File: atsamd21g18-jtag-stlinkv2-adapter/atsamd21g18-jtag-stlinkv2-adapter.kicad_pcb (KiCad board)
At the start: 2 copper layers, 31.8 x 35.6 mm, 4 parts, among them J1 JTAG, J2 HEADER-MALE-10POS-TH-2x5-P0.1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, J3 HEADER-MALE-5POS-TH-1x05-P0.1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, J4 HEADER-MALE-10POS-TH-2x5-P1.2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

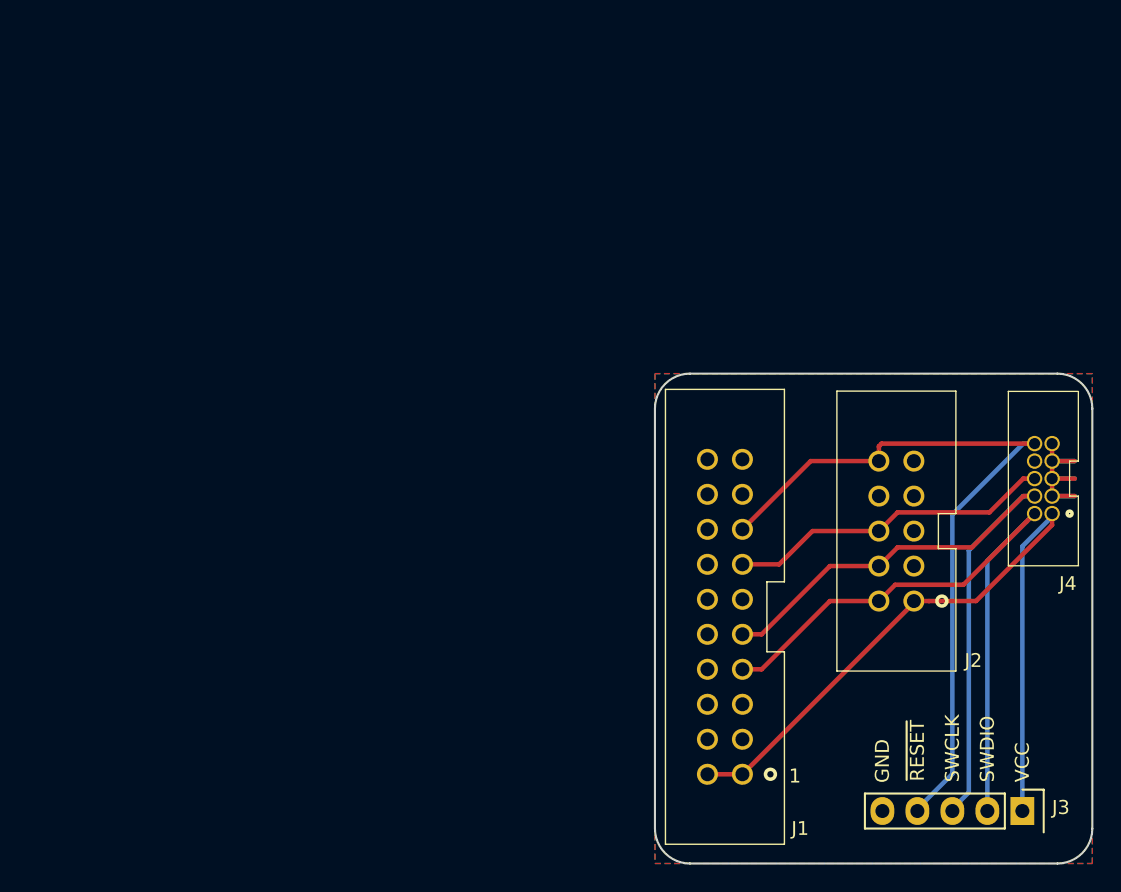
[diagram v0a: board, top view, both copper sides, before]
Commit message: Updating v1.0 with FabNotes file.
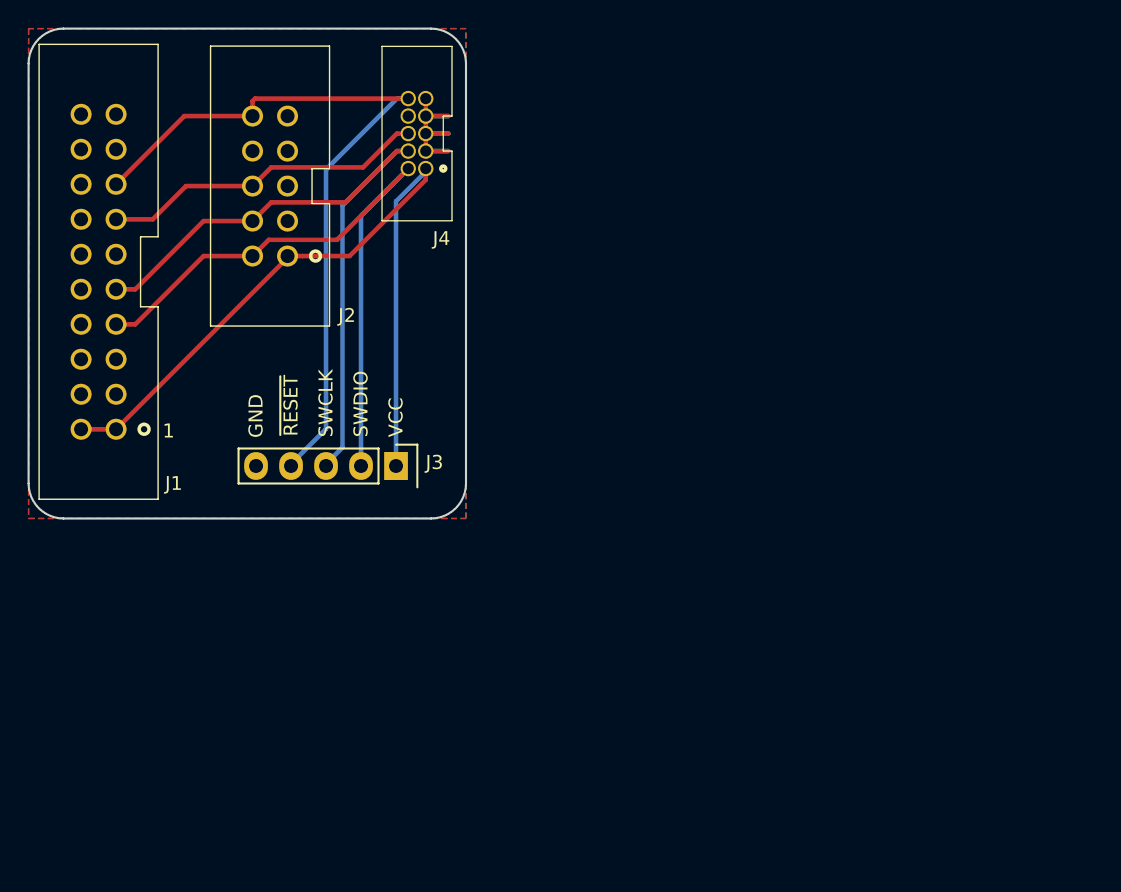
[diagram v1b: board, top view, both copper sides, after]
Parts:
- moved J2 51.9 mm to (45.7, 44.8)
- moved J3 51.9 mm to (54.9, 65.1)
- moved J4 51.9 mm to (56.4, 41.0)
- moved J1 51.9 mm to (33.3, 57.4)
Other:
- board text added: "FABRICATION NOTES 1. THIS IS A 2 LAYER BOARD. 2. EXTERNAL LAYERS SHALL HAVE 1 OZ COPPER. 3. MATERIAL: FR4 AND 0.062 INCH +/- 10% THICK. 4. BOARDS SHALL BE ROHS COMPLIANT. 5. MANUFACTURE IN ACCORDANCE WITH IPC-6012 CLASS 2 6. MASK: BOTH SIDES OF THE BOARD SHALL HAVE SOLDER MASK (ANY COLOR) OVER BARE COPPER. 7. SILK: BOTH SIDES OF THE BOARD SHALL HAVE WHITE SILKSCREEN. DO NOT PLACE SILK OVER BARE C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"
